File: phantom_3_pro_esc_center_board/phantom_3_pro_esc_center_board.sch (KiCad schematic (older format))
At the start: 59 parts, among them J1 CONN_BAT, J10 M1_BK, J11 M1_RD, J12 M1_YW, J13 M2_YW, J14 M2_RD, J15 M2_BK, J16 M3_BK, J17 M3_RD, J18 M3_YW, J19 M4_YW, J2 CONN_GPS, J20 M4_RD, J21 M4_BK, J3 CONN_GIMBAL, J4 CONN_CMPAS, J5 CONN_OFDM, J6 CONN_USB, J7 CONN_API, J8 CONN_MC_FRONT, J9 CONN_MC_BACK

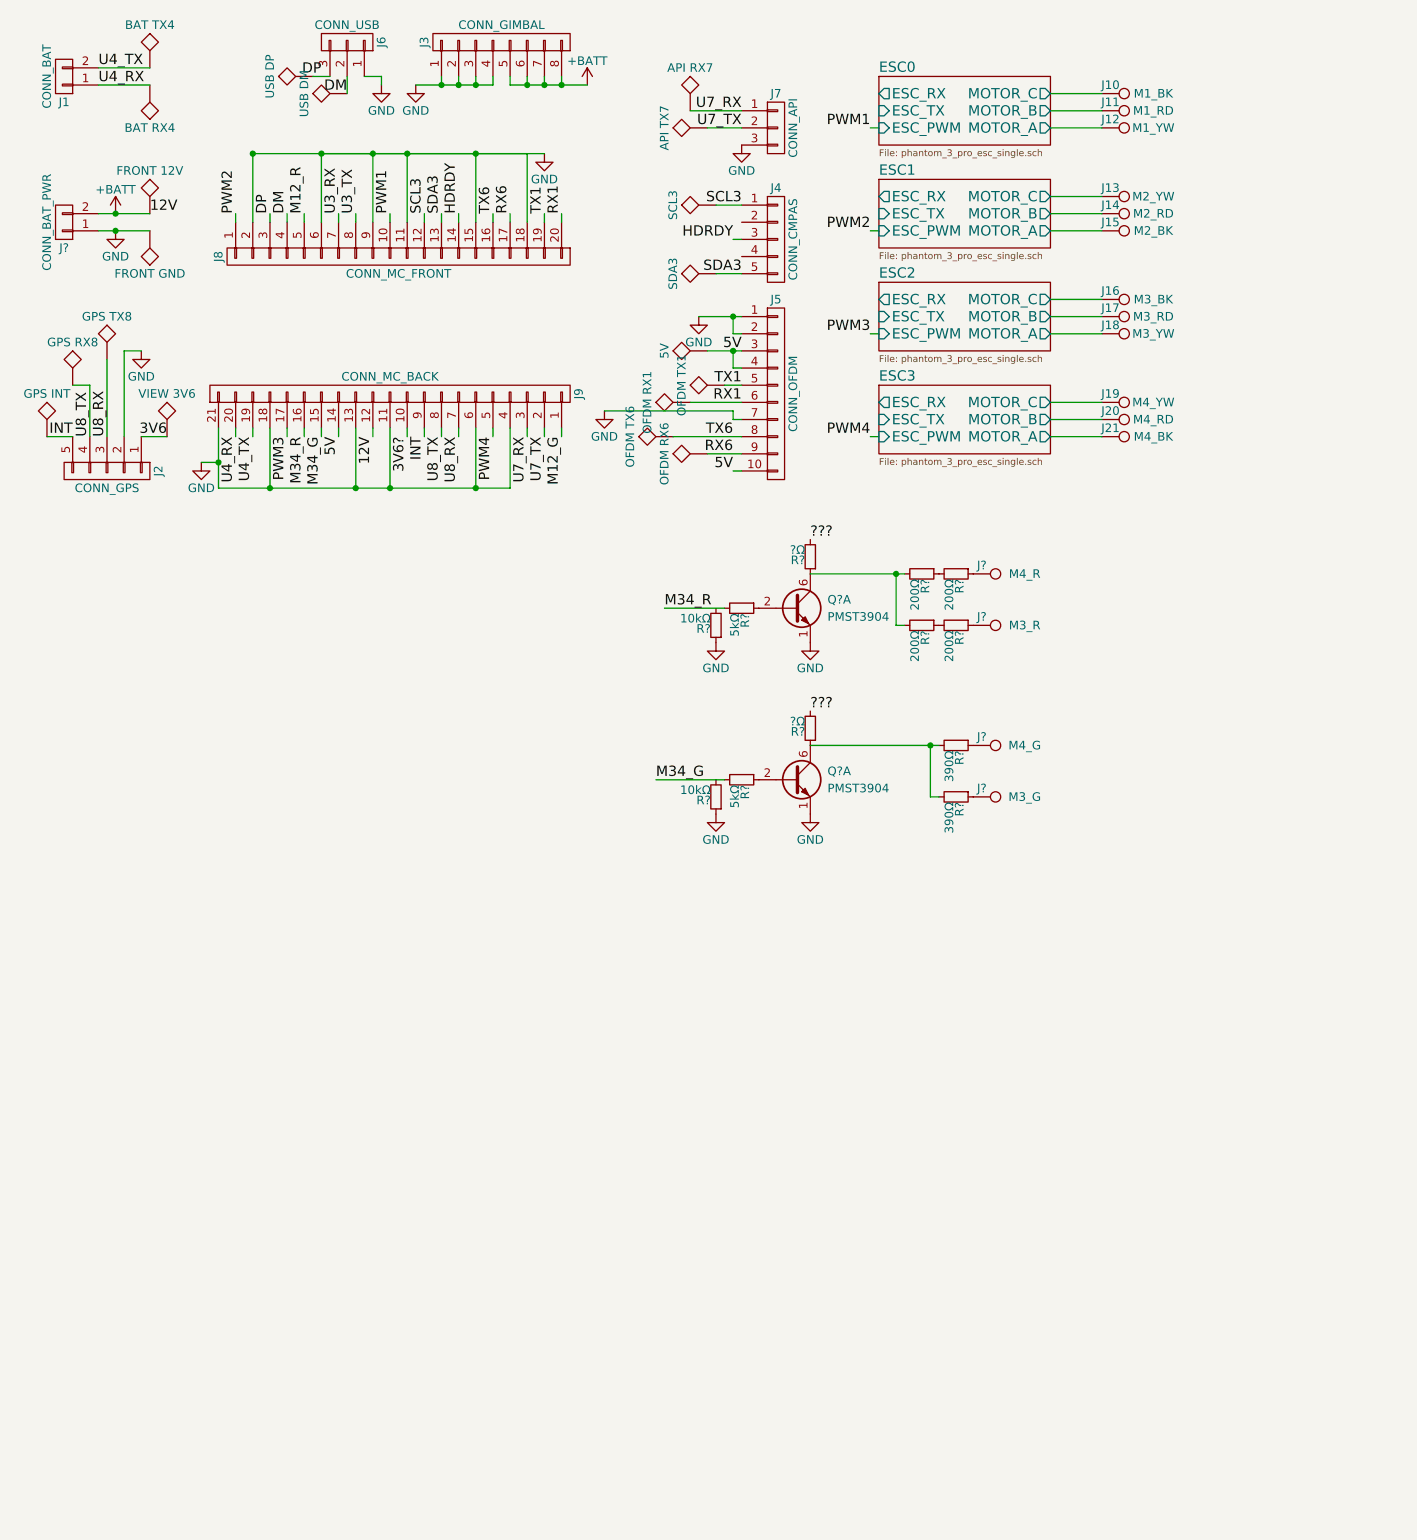
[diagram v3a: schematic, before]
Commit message: ESC Center: Added ESC connection to FC.
The ESC-FC connection is made through resistors,
so I haven't identified it in first check.
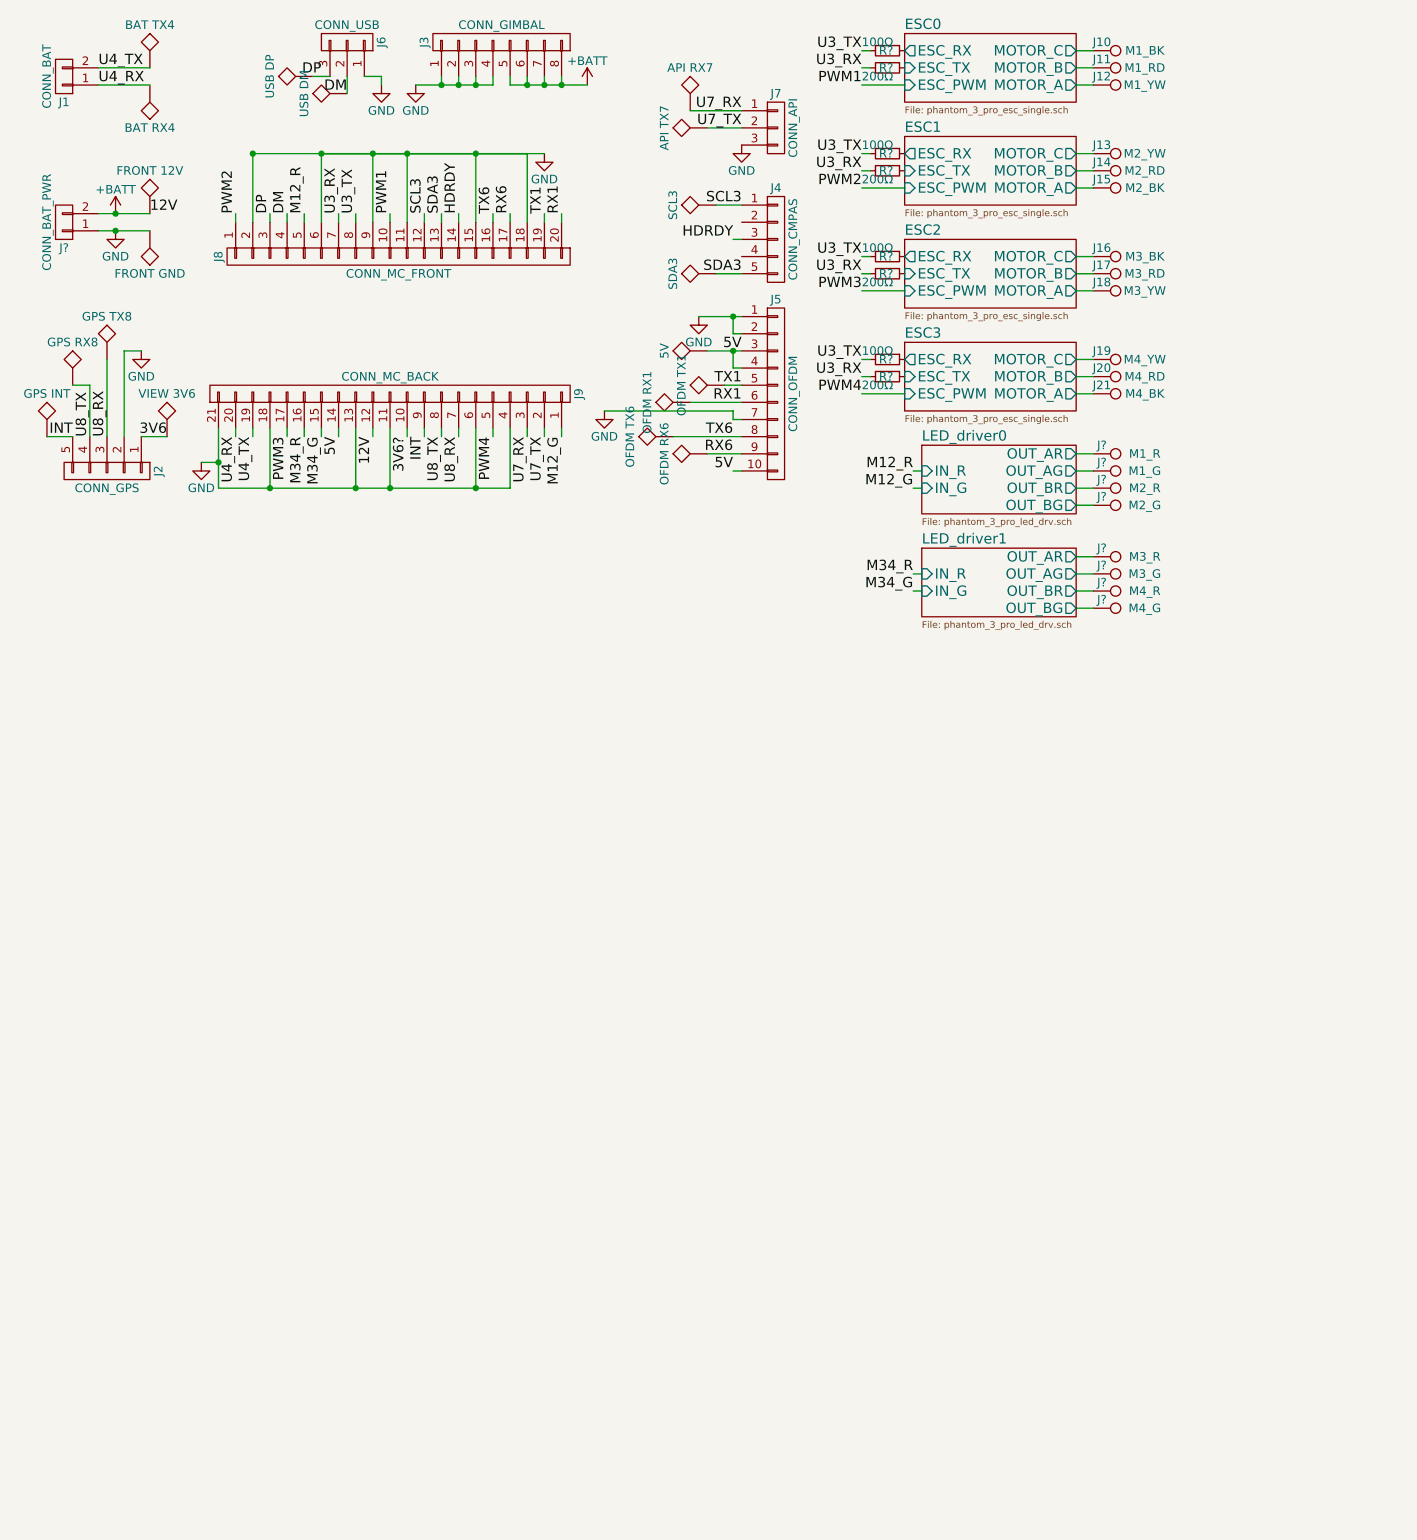
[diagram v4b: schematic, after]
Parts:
- removed Q? (x2): PMST3904, TO_SOT_Packages_SMD:SOT-363, symbol PMBT2222AYS
- removed R? (x4): 200Ω, symbol R_Small
- removed R? (x2): 390Ω, symbol R_Small
- removed R? (x2): 5kΩ, symbol R_Small
- removed R? (x2): 10kΩ, symbol R_Small
- removed R? (x2): ?Ω, symbol R_Small
- added J?: M4_R, symbol TEST_1P
- added J?: M4_G, symbol TEST_1P
- added J?: M3_R, symbol TEST_1P
- added J?: M3_G, symbol TEST_1P
- added R? (x4): 100Ω, symbol R_Small
- added R? (x4): 200Ω, symbol R_Small
- J?: value M4_R -> M2_R
- J?: value M4_G -> M2_G
- J?: value M3_R -> M1_R
- J?: value M3_G -> M1_G
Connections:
- net ESC0/ESC_RX: now also R?.1
- net ESC0/ESC_TX: now also R?.1
- net ESC1/ESC_RX: now also R?.1
- net ESC1/ESC_TX: now also R?.1
- net ESC2/ESC_RX: now also R?.1
- net ESC2/ESC_TX: now also R?.1
- net ESC3/ESC_RX: now also R?.1
- net ESC3/ESC_TX: now also R?.1
- net U3_RX: now also R?.2, R?.2, R?.2, R?.2
- net U3_TX: now also R?.2, R?.2, R?.2, R?.2
- net LED_driver0/OUT_BR: now reaches J?.1
- net LED_driver0/OUT_AR: now reaches J?.1
- net LED_driver0/OUT_BG: now reaches J?.1
- net LED_driver0/OUT_AG: now reaches J?.1
- new net LED_driver1/OUT_AG: J?.1
- new net LED_driver1/OUT_AR: J?.1
- new net LED_driver1/OUT_BG: J?.1
- new net LED_driver1/OUT_BR: J?.1
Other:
- moved on the sheet: J10, J11, J12, J13, J14, J15, J16, J17, J18, J19, J20, J21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

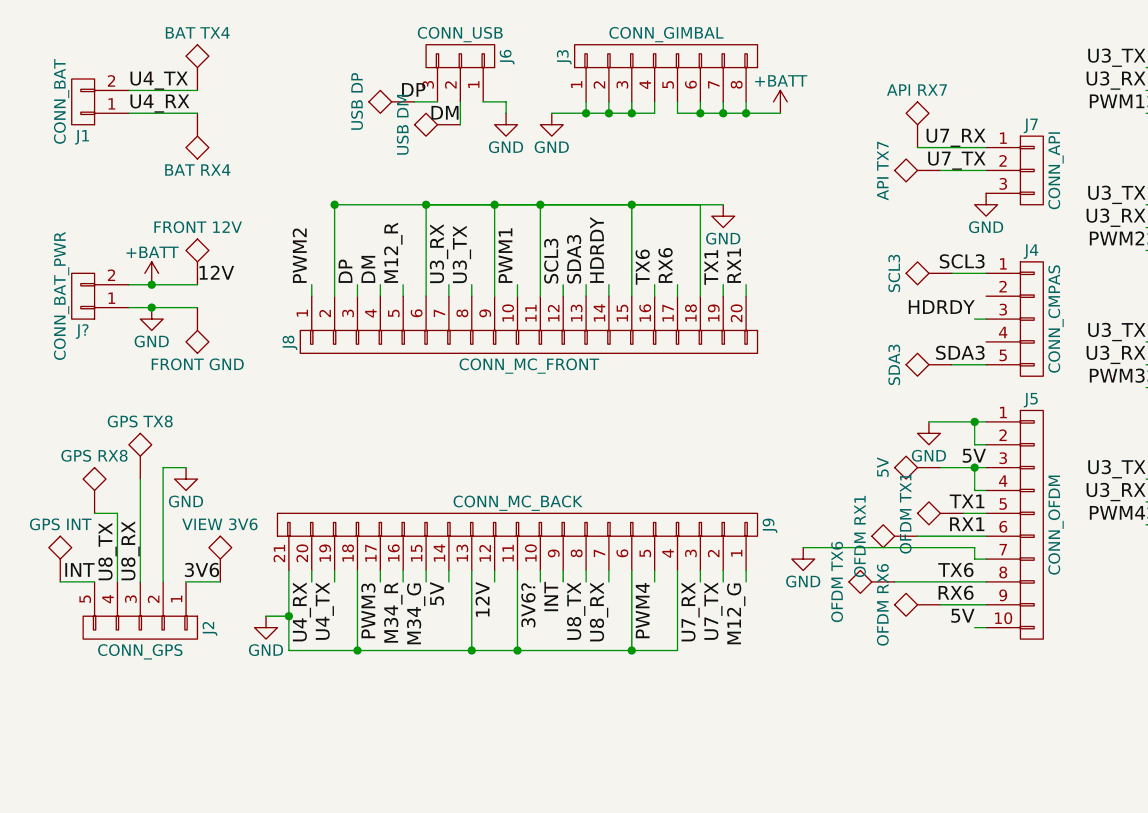
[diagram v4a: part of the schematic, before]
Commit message: ESC Center: Updated to latest findings.
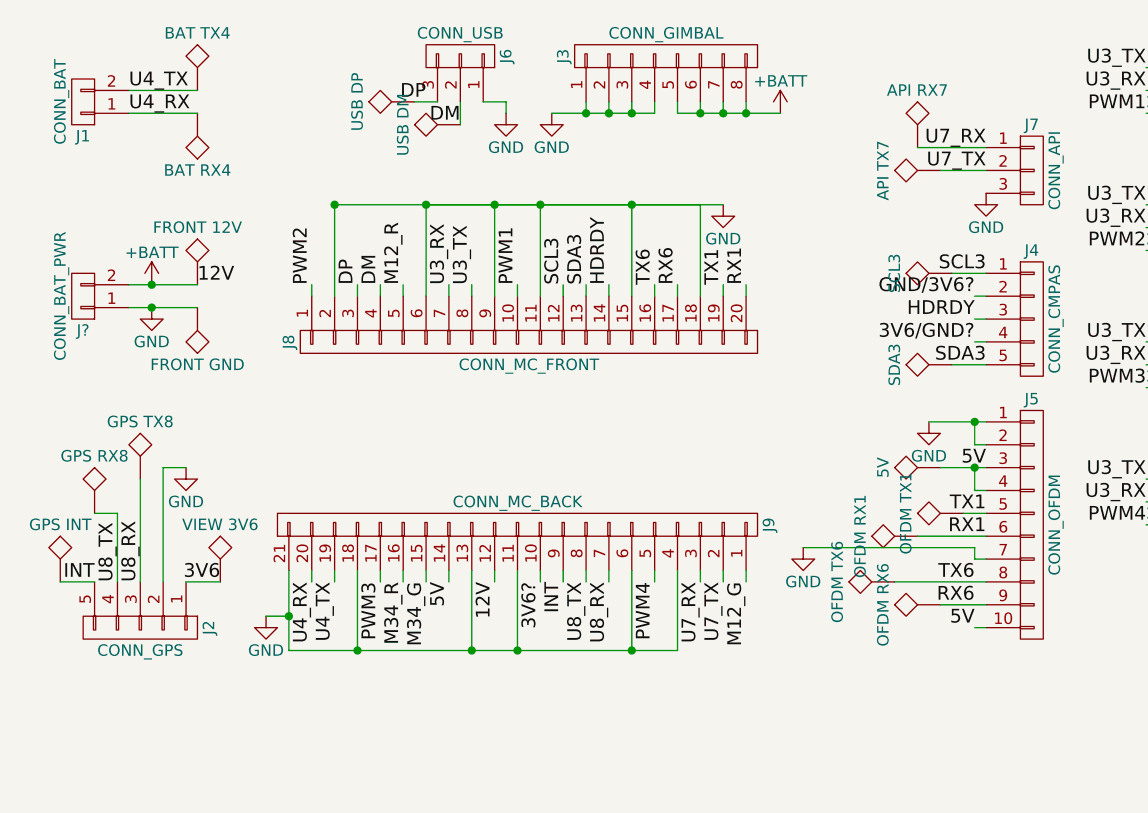
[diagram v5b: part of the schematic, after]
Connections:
- net GND/3V6?: now reaches J4.2 (P2)
- net 3V6/GND?: now reaches J4.4 (P4)
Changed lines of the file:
@@
 LIBS:DRV8301_DCA_56_thin
 LIBS:DRV8301_DCA_56
-LIBS:TMS320F28027FPT
 LIBS:motors
 LIBS:motor_drivers
+LIBS:texas-uc
 LIBS:phantom_3_pro_esc_center_board-cache
 EELAYER 25 0
@@
 	1750 2900 1750 2950
 Wire Wire Line
-	1650 2900 1650 3100
-Wire Wire Line
-	1650 3100 1650 3250
+	1650 2900 1650 3250
 Wire Wire Line
 	1750 1700 1750 1650
@@
 	2050 2950 2050 2900
 Wire Wire Line
-	1850 1300 2250 1300
-Wire Wire Line
-	2250 1300 2550 1300
-Wire Wire Line
-	2550 1300 2750 1300
-Wire Wire Line
-	2750 1300 3150 1300
-Wire Wire Line
-	3150 1300 3550 1300
-Wire Wire Line
-	2250 1300 2550 1300
-Wire Wire Line
-	2550 1300 2750 1300
-Wire Wire Line
-	2750 1300 3150 1300
-Wire Wire Line
-	3150 1300 3450 1300
+	1850 1300 3550 1300
+Wire Wire Line
+	2250 1300 3450 1300
 Wire Wire Line
 	2650 1700 2650 1650
@@
 $EndComp
 Wire Wire Line
-	2800 900  2950 900
-Wire Wire Line
-	2950 900  3050 900
-Wire Wire Line
-	3050 900  3150 900
-Wire Wire Line
-	3150 900  3250 900
+	2800 900  3250 900
 Wire Wire Line
 	3250 900  3250 850
@@
 	3350 850  3350 900
 Wire Wire Line
-	3350 900  3450 900
-Wire Wire Line
-	3450 900  3550 900
-Wire Wire Line
-	3550 900  3650 900
-Wire Wire Line
-	3650 900  3800 900
+	3350 900  3800 900
 Wire Wire Line
 	3650 850  3650 900
@@
 	2150 1700 2150 1650
 Wire Wire Line
-	1650 3250 1950 3250
-Wire Wire Line
-	1950 3250 2450 3250
-Wire Wire Line
-	2450 3250 2650 3250
-Wire Wire Line
-	2650 3250 3150 3250
-Wire Wire Line
-	3150 3250 3350 3250
+	1650 3250 3350 3250
 Connection ~ 1950 3250
 Connection ~ 2650 3250
@@
 $EndComp
 Wire Wire Line
-	4450 2250 4650 2250
-Wire Wire Line
-	4650 2250 4700 2250
+	4450 2250 4700 2250
 Wire Wire Line
 	4700 2350 4650 2350
@@
 5V
 Wire Wire Line
-	4500 2450 4650 2450
-Wire Wire Line
-	4650 2450 4700 2450
+	4500 2450 4700 2450
 Wire Wire Line
 	4700 2550 4650 2550
@@
 $EndComp
 Wire Wire Line
-	950  1650 1050 1650
-Wire Wire Line
-	1050 1650 1250 1650
-Wire Wire Line
-	950  1750 1050 1750
-Wire Wire Line
-	1050 1750 1250 1750
+	950  1650 1250 1650
+Wire Wire Line
+	950  1750 1250 1750
 Text Label 1250 1650 0    60   ~ 0
 12V
@@
 	0    1    1    0
 $EndComp
+Text Label 4650 1700 2    60   ~ 0
+GND/3V6?
+Wire Wire Line
+	4700 1700 4650 1700
+Text Label 4650 1900 2    60   ~ 0
+3V6/GND?
+Wire Wire Line
+	4700 1900 4650 1900
 $EndSCHEMATC
